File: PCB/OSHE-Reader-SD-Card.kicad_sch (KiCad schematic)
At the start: 0 parts

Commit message: started work adding hierarchical power pins to mcu and sd card sheets
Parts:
- added J2: 112L-TDA0, CONN_112L-TDA0_ATT, symbol 112L_TDA0:112L-TDA0
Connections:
- new net 3V3: J2.4 (VDD)
- new net CS: J2.2 (CD/DAT3)
- new net GND: J2.19 (GND), J2.20 (GND), J2.21 (GND), J2.22 (GND), J2.23 (GND), J2.6 (VSS)
- no-connect marks 0 -> 11

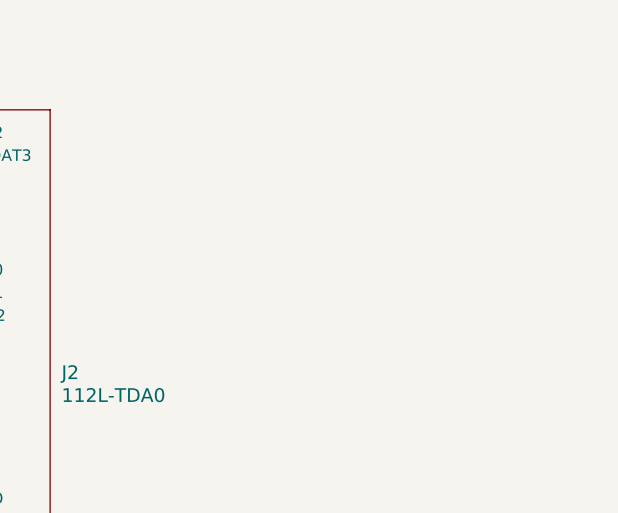
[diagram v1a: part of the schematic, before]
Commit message: Update OSHE-Reader-SD-Card.kicad_sch
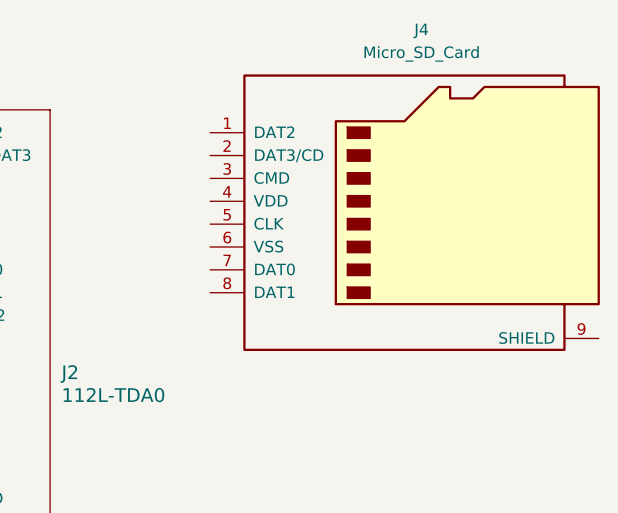
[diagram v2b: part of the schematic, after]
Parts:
- added J4: Micro_SD_Card, symbol Connector:Micro_SD_Card
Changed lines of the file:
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@@
+		)
+	)
+	(symbol
+		(lib_id "Connector:Micro_SD_Card")
+		(at 130.81 57.15 0)
+		(unit 1)
+		(exclude_from_sim no)
+		(in_bom yes)
+		(on_board yes)
+		(dnp no)
+		(fields_autoplaced yes)
+		(property "Reference" "J4"
+			(at 131.445 38.1 0)
+			(effects
+				(font
+					(size 1.27 1.27)
+				)
+			)
+		)
+		(property "Value" "Micro_SD_Card"
+			(at 131.445 40.64 0)
+			(effects
+				(font
+					(size 1.27 1.27)
+				)
+			)
+		)
+		(property "Footprint" ""
+			(at 160.02 49.53 0)
+			(effects
+				(font
+					(size 1.27 1.27)
+				)
+				(hide yes)
+			)
+		)
+		(property "Datasheet" "https://www.we-online.com/components/products/datasheet/693072010801.pdf"
+			(at 130.81 57.15 0)
+			(effects
+				(font
+					(size 1.27 1.27)
+				)
+				(hide yes)
+			)
+		)
+		(property "Description" "Micro SD Card Socket"
+			(at 130.81 57.15 0)
+			(effects
+				(font
+					(size 1.27 1.27)
+				)
+				(hide yes)
+			)
+		)
+		(pin "1"
+		)
+		(pin "7"
+		)
+		(pin "6"
+		)
+		(pin "4"
+		)
+		(pin "5"
+		)
+		(pin "2"
+		)
+		(pin "3"
+		)
+		(pin "8"
+		)
+		(pin "9"
+		)
+		(instances
+			(project ""
+				(path "/3f072c92-e35a-4654-839b-728bd3dc3a46/f673c940-d558-4160-83eb-d33ca6356616"
+					(reference "J4")
+					(unit 1)
+				)
+			)
 		)
 	)

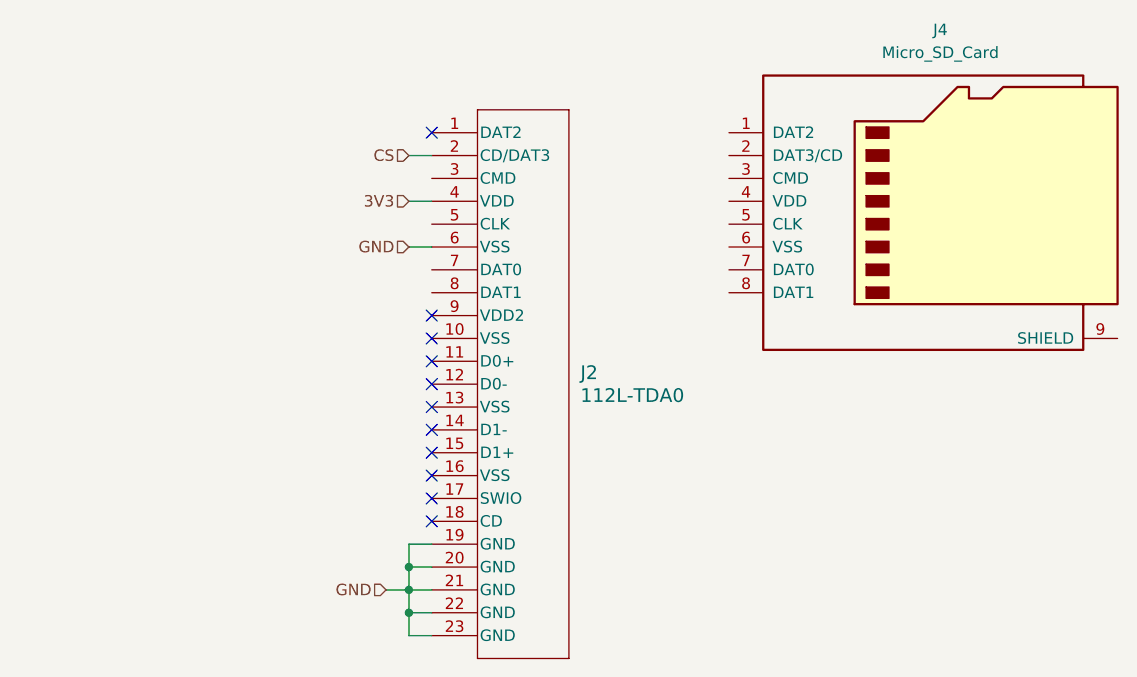
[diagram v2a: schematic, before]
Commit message: sd card *should* be done with the exception of things like decoupling caps
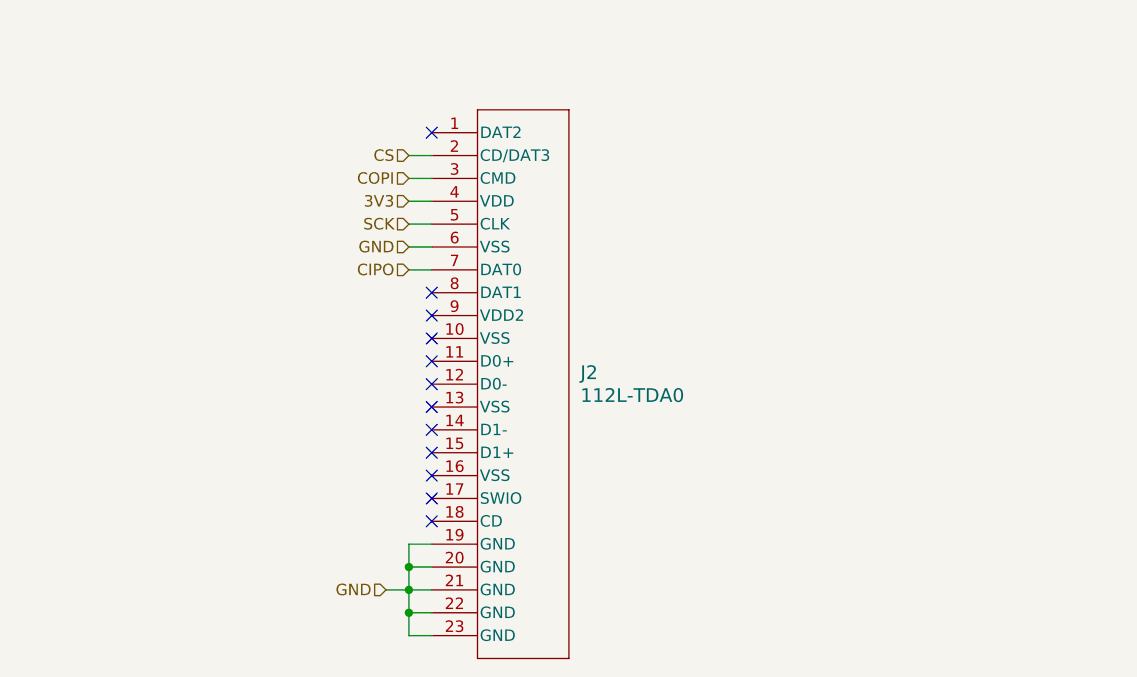
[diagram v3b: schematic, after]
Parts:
- removed J4: Micro_SD_Card, symbol Connector:Micro_SD_Card
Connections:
- net COPI: now reaches J2.3 (CMD)
- net SCK: now reaches J2.5 (CLK)
- net CIPO: now reaches J2.7 (DAT0)
- no-connect marks 11 -> 12
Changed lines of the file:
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@@
+	)
+	(no_connect
+		(at 74.93 67.31)
 	)
 	(no_connect
@@
 	(wire
 		(pts
+			(xy 72.39 59.69) (xy 74.93 59.69)
+		)
+		(stroke
+			(width 0)
+			(type default)
+		)
+	)
+	(wire
+		(pts
 			(xy 74.93 102.87) (xy 72.39 102.87)
 		)
@@
 	(wire
 		(pts
+			(xy 72.39 54.61) (xy 74.93 54.61)
+		)
+		(stroke
+			(width 0)
+			(type default)
+		)
+	)
+	(wire
+		(pts
 			(xy 72.39 95.25) (xy 72.39 97.79)
 		)
@@
 	(wire
 		(pts
+			(xy 72.39 64.77) (xy 74.93 64.77)
+		)
+		(stroke
+			(width 0)
+			(type default)
+		)
+	)
+	(wire
+		(pts
 			(xy 72.39 97.79) (xy 72.39 100.33)
 		)
@@
 		)
 	)
+	(hierarchical_label "CIPO"
+		(shape input)
+		(at 72.39 64.77 180)
+		(effects
+			(font
+				(size 1.27 1.27)
+			)
+			(justify right)
+		)
+	)
+	(hierarchical_label "COPI"
+		(shape input)
+		(at 72.39 54.61 180)
+		(effects
+			(font
+				(size 1.27 1.27)
+			)
+			(justify right)
+		)
+	)
 	(hierarchical_label "3V3"
 		(shape input)
 		(at 72.39 57.15 180)
+		(effects
+			(font
+				(size 1.27 1.27)
+			)
+			(justify right)
+		)
+	)
+	(hierarchical_label "SCK"
+		(shape input)
+		(at 72.39 59.69 180)
 		(effects
 			(font
@@
 					(unit 1)
 				)
-			)
-		)
-	)
-	(symbol
-		(lib_id "Connector:Micro_SD_Card")
-		(at 130.81 57.15 0)
-		(unit 1)
-		(exclude_from_sim no)
-		(in_bom yes)
-		(on_board yes)
-		(dnp no)
-		(fields_autoplaced yes)
-		(property "Reference" "J4"
-			(at 131.445 38.1 0)
-			(effects
-				(font
-					(size 1.27 1.27)
-				)
-			)
-		)
-		(property "Value" "Micro_SD_Card"
-			(at 131.445 40.64 0)
-			(effects
-				(font
-					(size 1.27 1.27)
-				)
-			)
-		)
-		(property "Footprint" ""
-			(at 160.02 49.53 0)
-			(effects
-				(font
-					(size 1.27 1.27)
-				)
-				(hide yes)
-			)
-		)
-		(property "Datasheet" "https://www.we-online.com/components/products/datasheet/693072010801.pdf"
-			(at 130.81 57.15 0)
-			(effects
-				(font
-					(size 1.27 1.27)
-				)
-				(hide yes)
-			)
-		)
-		(property "Description" "Micro SD Card Socket"
-			(at 130.81 57.15 0)
-			(effects
-				(font
-					(size 1.27 1.27)
-				)
-				(hide yes)
-			)
-		)
-		(pin "1"
-		)
-		(pin "7"
-		)
-		(pin "6"
-		)
-		(pin "4"
-		)
-		(pin "5"
-		)
-		(pin "2"
-		)
-		(pin "3"
-		)
-		(pin "8"
-		)
-		(pin "9"
-		)
-		(instances
-			(project ""
-				(path "/3f072c92-e35a-4654-839b-728bd3dc3a46/f673c940-d558-4160-83eb-d33ca6356616"
-					(reference "J4")
-					(unit 1)
-				)

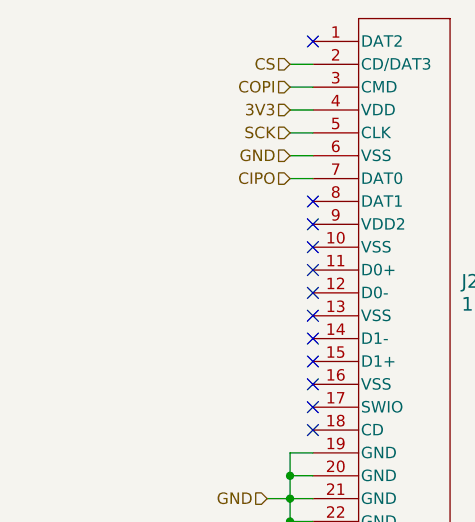
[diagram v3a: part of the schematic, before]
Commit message: added decoupling cap to sd card socket
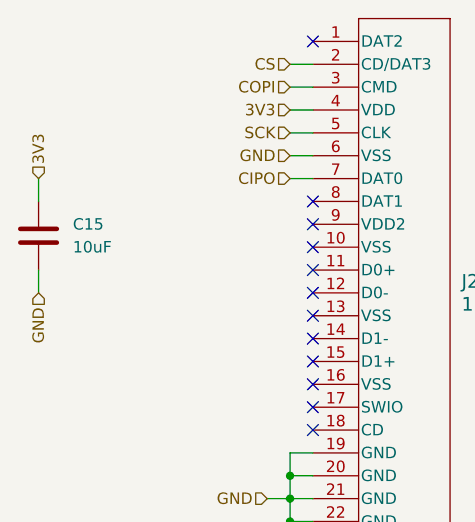
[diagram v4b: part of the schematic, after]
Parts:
- added C15: 10uF, symbol Device:C
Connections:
- net 3V3: now also C15.1
- net GND: now also C15.2
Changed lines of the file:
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@@
+	(wire
+		(pts
+			(xy 44.45 74.93) (xy 44.45 77.47)
+		)
+		(stroke
+			(width 0)
+			(type default)
+		)
+	)
 	(wire
 		(pts
@@
 	(wire
 		(pts
+			(xy 44.45 64.77) (xy 44.45 67.31)
+		)
+		(stroke
+			(width 0)
+			(type default)
+		)
+	)
+	(wire
+		(pts
 			(xy 72.39 105.41) (xy 74.93 105.41)
 		)
@@
 		)
 	)
+	(hierarchical_label "3V3"
+		(shape input)
+		(at 44.45 64.77 90)
+		(effects
+			(font
+				(size 1.27 1.27)
+			)
+			(justify left)
+		)
+	)
 	(hierarchical_label "GND"
 		(shape input)
@@
 		(shape input)
 		(at 69.85 100.33 180)
+		(effects
+			(font
+				(size 1.27 1.27)
+			)
+			(justify right)
+		)
+	)
+	(hierarchical_label "GND"
+		(shape input)
+		(at 44.45 77.47 270)
 		(effects
 			(font
@@
 					(unit 1)
 				)
+			)
+		)
+	)
+	(symbol
+		(lib_id "Device:C")
+		(at 44.45 71.12 0)
+		(unit 1)
+		(exclude_from_sim no)
+		(in_bom yes)
+		(on_board yes)
+		(dnp no)
+		(fields_autoplaced yes)
+		(property "Reference" "C15"
+			(at 48.26 69.8499 0)
+			(effects
+				(font
+					(size 1.27 1.27)
+				)
+				(justify left)
+			)
+		)
+		(property "Value" "10uF"
+			(at 48.26 72.3899 0)
+			(effects
+				(font
+					(size 1.27 1.27)
+				)
+				(justify left)
+			)
+		)
+		(property "Footprint" ""
+			(at 45.4152 74.93 0)
+			(effects
+				(font
+					(size 1.27 1.27)
+				)
+				(hide yes)
+			)
+		)
+		(property "Datasheet" "~"
+			(at 44.45 71.12 0)
+			(effects
+				(font
+					(size 1.27 1.27)
+				)
+				(hide yes)
+			)
+		)
+		(property "Description" "Unpolarized capacitor"
+			(at 44.45 71.12 0)
+			(effects
+				(font
+					(size 1.27 1.27)
+				)
+				(hide yes)
+			)
+		)
+		(pin "1"
+		)
+		(pin "2"
+		)
+		(instances
+			(project ""
+				(path "/3f072c92-e35a-4654-839b-728bd3dc3a46/f673c940-d558-4160-83eb-d33ca6356616"
+					(reference "C15")
+					(unit 1)
+				)

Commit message: HOPEFULLY GOOD FOR EVER (good for first semester) :)
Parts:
- added C24: 0.1uF, symbol Device:C
- J2: footprint CONN_112L-TDA0_ATT -> 112L_TDA0:CONN_112L-TDA0_ATT
- renumbered C15 to C25
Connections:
- net 3V3: now also C24.1
- net GND: now also C24.2
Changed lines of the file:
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@@
+	(wire
+		(pts
+			(xy 39.37 67.31) (xy 39.37 64.77)
+		)
+		(stroke
+			(width 0)
+			(type default)
+		)
+	)
 	(wire
 		(pts
@@
 	(wire
 		(pts
+			(xy 39.37 77.47) (xy 44.45 77.47)
+		)
+		(stroke
+			(width 0)
+			(type default)
+		)
+	)
+	(wire
+		(pts
 			(xy 69.85 100.33) (xy 72.39 100.33)
 		)
@@
 	(wire
 		(pts
+			(xy 39.37 64.77) (xy 44.45 64.77)
+		)
+		(stroke
+			(width 0)
+			(type default)
+		)
+	)
+	(wire
+		(pts
 			(xy 72.39 52.07) (xy 74.93 52.07)
 		)
@@
 	(wire
 		(pts
+			(xy 39.37 74.93) (xy 39.37 77.47)
+		)
+		(stroke
+			(width 0)
+			(type default)
+		)
+	)
+	(wire
+		(pts
 			(xy 72.39 59.69) (xy 74.93 59.69)
 		)
@@
 	)
 	(hierarchical_label "CIPO"
-		(shape input)
+		(shape output)
 		(at 72.39 64.77 180)
 		(effects
@@
 			)
 			(justify right)
+		)
+	)
+	(symbol
+		(lib_id "Device:C")
+		(at 39.37 71.12 0)
+		(mirror y)
+		(unit 1)
+		(exclude_from_sim no)
+		(in_bom yes)
+		(on_board yes)
+		(dnp no)
+		(property "Reference" "C24"
+			(at 35.56 69.8499 0)
+			(effects
+				(font
+					(size 1.27 1.27)
+				)
+				(justify left)
+			)
+		)
+		(property "Value" "0.1uF"
+			(at 35.56 72.3899 0)
+			(effects
+				(font
+					(size 1.27 1.27)
+				)
+				(justify left)
+			)
+		)
+		(property "Footprint" ""
+			(at 38.4048 74.93 0)
+			(effects
+				(font
+					(size 1.27 1.27)
+				)
+				(hide yes)
+			)
+		)
+		(property "Datasheet" "~"
+			(at 39.37 71.12 0)
+			(effects
+				(font
+					(size 1.27 1.27)
+				)
+				(hide yes)
+			)
+		)
+		(property "Description" "Unpolarized capacitor"
+			(at 39.37 71.12 0)
+			(effects
+				(font
+					(size 1.27 1.27)
+				)
+				(hide yes)
+			)
+		)
+		(pin "1"
+		)
+		(pin "2"
+		)
+		(instances
+			(project "OSHE-Reader-PCB"
+				(path "/3f072c92-e35a-4654-839b-728bd3dc3a46/f673c940-d558-4160-83eb-d33ca6356616"
+					(reference "C24")
+					(unit 1)
+				)
+			)
 		)
 	)
@@
 			)
 		)
-		(property "Footprint" "CONN_112L-TDA0_ATT"
+		(property "Footprint" "112L_TDA0:CONN_112L-TDA0_ATT"
 			(at 69.85 49.53 0)
 			(effects
@@
 		(dnp no)
 		(fields_autoplaced yes)
-		(property "Reference" "C15"
+		(property "Reference" "C25"
 			(at 48.26 69.8499 0)
 			(effects
@@
 			(project ""
 				(path "/3f072c92-e35a-4654-839b-728bd3dc3a46/f673c940-d558-4160-83eb-d33ca6356616"
-					(reference "C15")
+					(reference "C25")
 					(unit 1)
 				)

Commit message: small
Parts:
- removed C24: 0.1uF, symbol Device:C
- J2: footprint 112L_TDA0:CONN_112L-TDA0_ATT -> CONN_112L-TDA0_ATT
- renumbered C25 to C15
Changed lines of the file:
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@@
-	(wire
-		(pts
-			(xy 39.37 67.31) (xy 39.37 64.77)
-		)
-		(stroke
-			(width 0)
-			(type default)
-		)
-	)
 	(wire
 		(pts
@@
 	(wire
 		(pts
-			(xy 39.37 77.47) (xy 44.45 77.47)
-		)
-		(stroke
-			(width 0)
-			(type default)
-		)
-	)
-	(wire
-		(pts
 			(xy 69.85 100.33) (xy 72.39 100.33)
 		)
@@
 	(wire
 		(pts
-			(xy 39.37 64.77) (xy 44.45 64.77)
-		)
-		(stroke
-			(width 0)
-			(type default)
-		)
-	)
-	(wire
-		(pts
 			(xy 72.39 52.07) (xy 74.93 52.07)
 		)
@@
 	(wire
 		(pts
-			(xy 39.37 74.93) (xy 39.37 77.47)
-		)
-		(stroke
-			(width 0)
-			(type default)
-		)
-	)
-	(wire
-		(pts
 			(xy 72.39 59.69) (xy 74.93 59.69)
 		)
@@
 	)
 	(hierarchical_label "CIPO"
-		(shape output)
+		(shape input)
 		(at 72.39 64.77 180)
 		(effects
@@
 			)
 			(justify right)
-		)
-	)
-	(symbol
-		(lib_id "Device:C")
-		(at 39.37 71.12 0)
-		(mirror y)
-		(unit 1)
-		(exclude_from_sim no)
-		(in_bom yes)
-		(on_board yes)
-		(dnp no)
-		(property "Reference" "C24"
-			(at 35.56 69.8499 0)
-			(effects
-				(font
-					(size 1.27 1.27)
-				)
-				(justify left)
-			)
-		)
-		(property "Value" "0.1uF"
-			(at 35.56 72.3899 0)
-			(effects
-				(font
-					(size 1.27 1.27)
-				)
-				(justify left)
-			)
-		)
-		(property "Footprint" ""
-			(at 38.4048 74.93 0)
-			(effects
-				(font
-					(size 1.27 1.27)
-				)
-				(hide yes)
-			)
-		)
-		(property "Datasheet" "~"
-			(at 39.37 71.12 0)
-			(effects
-				(font
-					(size 1.27 1.27)
-				)
-				(hide yes)
-			)
-		)
-		(property "Description" "Unpolarized capacitor"
-			(at 39.37 71.12 0)
-			(effects
-				(font
-					(size 1.27 1.27)
-				)
-				(hide yes)
-			)
-		)
-		(pin "1"
-		)
-		(pin "2"
-		)
-		(instances
-			(project "OSHE-Reader-PCB"
-				(path "/3f072c92-e35a-4654-839b-728bd3dc3a46/f673c940-d558-4160-83eb-d33ca6356616"
-					(reference "C24")
-					(unit 1)
-				)
-			)
 		)
 	)
@@
 			)
 		)
-		(property "Footprint" "112L_TDA0:CONN_112L-TDA0_ATT"
+		(property "Footprint" "CONN_112L-TDA0_ATT"
 			(at 69.85 49.53 0)
 			(effects
@@
 		(dnp no)
 		(fields_autoplaced yes)
-		(property "Reference" "C25"
+		(property "Reference" "C15"
 			(at 48.26 69.8499 0)
 			(effects
@@
 			(project ""
 				(path "/3f072c92-e35a-4654-839b-728bd3dc3a46/f673c940-d558-4160-83eb-d33ca6356616"
-					(reference "C25")
+					(reference "C15")
 					(unit 1)
 				)

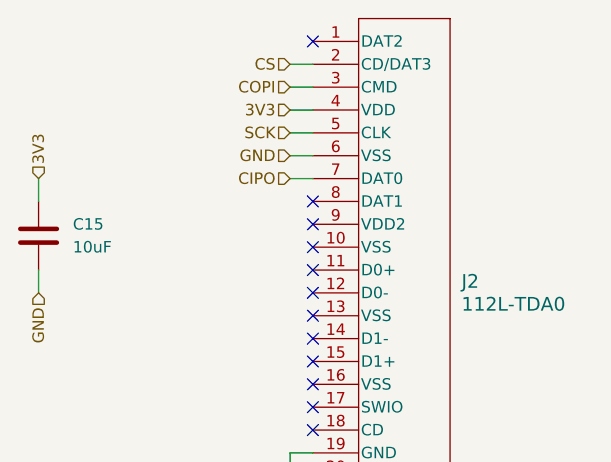
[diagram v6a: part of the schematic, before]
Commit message: sheet pins for SD card module
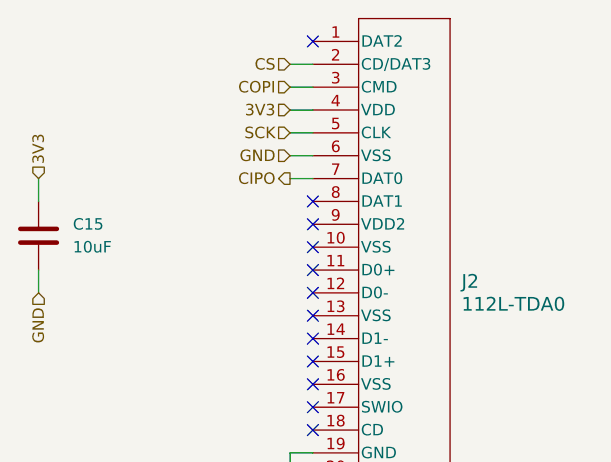
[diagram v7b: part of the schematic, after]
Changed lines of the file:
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@@
 	)
 	(hierarchical_label "CIPO"
-		(shape input)
+		(shape output)
 		(at 72.39 64.77 180)
 		(effects

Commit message: Updates reader display connector
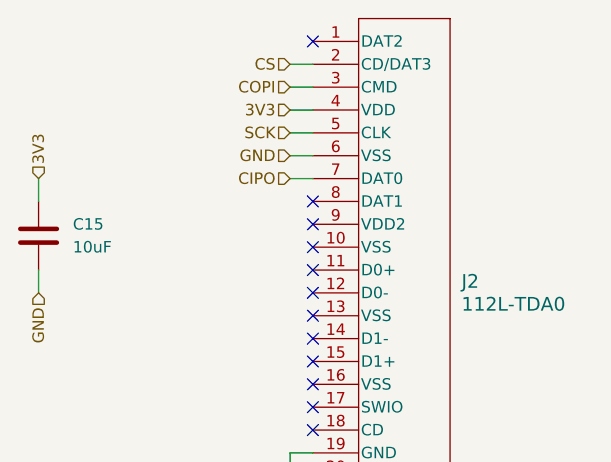
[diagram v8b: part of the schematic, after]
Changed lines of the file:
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@@
 	)
 	(hierarchical_label "CIPO"
-		(shape output)
+		(shape input)
 		(at 72.39 64.77 180)
 		(effects
